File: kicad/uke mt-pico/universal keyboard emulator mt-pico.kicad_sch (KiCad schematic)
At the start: 0 parts

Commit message: first pcb floorplan
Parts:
- added C1, C2, C3, C6, C8: 10u, Capacitor_SMD:C_0805_2012Metric, symbol My Library:C_0805
- added C5: 100u, Capacitor_THT:CP_Radial_D5.0mm_P2.50mm, symbol Device:C_Polarized_Small
- added C7: 100n, Capacitor_SMD:C_0805_2012Metric, symbol My Library:C_0805
- added D1: L, LED_SMD:LED_1206_3216Metric, symbol My Library:D_1206
- added D2: +3V3, LED_SMD:LED_1206_3216Metric, symbol My Library:D_1206
- added D3: +5V, LED_SMD:LED_1206_3216Metric, symbol My Library:D_1206
- added D4: SM4001, Diode_SMD:D_SMA_Handsoldering, symbol Diode:SM4001
- added D5, D6, D7: NSVR0320MW2T1G, Diode_SMD:D_SOD-323_HandSoldering, symbol Diode:SM4001
- added H1, H2, H3, H4: MountingHole, MountingHole:MountingHole_2.2mm_M2, symbol Mechanical:MountingHole
- added J1: Mode Select, Connector_PinHeader_2.54mm:PinHeader_1x03_P2.54mm_Vertical, symbol Connector_Generic:Conn_01x03
- added J2: OLED Adapter, Connector_PinSocket_2.54mm:PinSocket_1x04_P2.54mm_Vertical, symbol Connector_Generic:Conn_01x04
- added J3: Serial, Connector_PinHeader_2.54mm:PinHeader_1x05_P2.54mm_Vertical, symbol Connector_Generic:Conn_01x05
- added J4: Conn_02x20_Odd_Even, Connector_PinHeader_2.54mm:PinHeader_2x20_P2.54mm_Vertical, symbol Connector_Generic:Conn_02x20_Odd_Even
- added J5: SWD, SAMTEC_FTSH-105-XX-X-DV, symbol FTSH-105-XX-X-DV:FTSH-105-XX-X-DV
- added J6: Pico VBUS, Connector_PinHeader_2.54mm:PinHeader_1x02_P2.54mm_Vertical, symbol Connector_Generic:Conn_01x02
- added R1, R9: 1M, Resistor_SMD:R_0805_2012Metric, symbol My Library:R_0805
- added R2, R3, R4: 1k, Resistor_SMD:R_0805_2012Metric, symbol My Library:R_0805
- added R5, R6, R7, R8: 10k, Resistor_SMD:R_0805_2012Metric, symbol My Library:R_0805
- added SW1: Reset Pico, Button_Switch_SMD:SW_SPST_PTS810, symbol Switch:SW_SPST
- added TP1, TP2, TP3: TestPoint_Harwin, My Libraries:Harwin-S1751-46-Test-Point, symbol My Library:TestPoint_Harwin
- added U1: MT8816, Package_DIP:DIP-40_W15.24mm_Socket_LongPads, symbol My Library:MT8816_40-Pin_DIP
- added U2, U3: 74HCT245, Package_SO:SOIC-20W_7.5x12.8mm_P1.27mm, symbol 74xx:74HC245
- added U4: Pico, My Libraries:RPi_Pico_W_Combined_SMD_TH, symbol RPi_Pico:Pico
- added U5: 74HCT595-VERIFY-FOOTPRINT, Package_SO:SO-16_3.9x9.9mm_P1.27mm, symbol 74xx:74HC595
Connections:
- new net: D3.1 (K), R4.1
- new net: R6.2, U3.1 (A->B)
- new net: D7.1 (K), U3.20 (VCC)
- new net: D2.1 (K), R3.1
- new net: D1.1 (K), R2.1
- new net: D6.1 (K), U2.20 (VCC)
- new net: D5.1 (K), U5.10 (~{SRCLR}), U5.16 (VCC)
- new net: R5.2, U2.1 (A->B)
- new net +3V3: C7.1, D2.2 (A), J4.38 (Pin_38), J5.01, U4.36 (3V3)
- new net +5V: C1.1, C2.1, C3.1, C5.1, C6.1, C8.1, D3.2 (A), D4.2 (A), D5.2 (A), D6.2 (A), D7.2 (A), J4.1 (Pin_1), J4.2 (Pin_2), R1.1, R7.1, R8.1, U1.40 (VDD)
- new net +5VA: D4.1 (K), J2.2 (Pin_2), J6.1 (Pin_1), U4.40 (VBUS)
- new net 245s_CE: R7.2, R8.2, U2.19 (CE), U3.19 (CE), U4.11 (GPIO8)
- new net 595_CLK: U4.5 (GPIO3), U5.11 (SRCLK)
- new net 595_DATA: U4.4 (GPIO2), U5.14 (SER)
- new net 595_Latch: U4.10 (GPIO7), U5.12 (RCLK)
- new net ADID: J4.37 (Pin_37), U4.32 (GPIO27_ADC1)
- new net AX0: U1.5 (AX0), U2.6 (A4)
- new net AX1: U1.22 (AX1), U2.3 (A1)
- new net AX2: U1.23 (AX2), U2.2 (A0)
- new net AX3: U1.4 (AX3), U2.7 (A5)
- new net AY0: U1.24 (AY0), U2.4 (A2)
- new net AY1: U1.25 (AY1), U2.5 (A3)
- new net AY2: U1.2 (AY2), U2.9 (A7)
- new net COL0: J4.3 (Pin_3), U1.33 (X0)
- new net COL1: J4.5 (Pin_5), U1.32 (X1)
- new net COL10: J4.25 (Pin_25), U1.12 (X10)
- new net COL11: J4.27 (Pin_27), U1.13 (X11)
- new net COL12: J4.29 (Pin_29), U1.27 (X12)
- new net COL13: J4.31 (Pin_31), U1.26 (X13)
- new net COL14: J4.33 (Pin_33), U1.6 (X14)
- new net COL15: J4.35 (Pin_35), U1.7 (X15)
- new net COL2: J4.7 (Pin_7), U1.31 (X2)
- new net COL3: J4.9 (Pin_9), U1.30 (X3)
- new net COL4: J4.11 (Pin_11), U1.29 (X4)
- new net COL5: J4.13 (Pin_13), U1.28 (X5)
- new net COL6: J4.15 (Pin_15), U1.8 (X6)
- new net COL7: J4.17 (Pin_17), U1.9 (X7)
- new net COL8: J4.21 (Pin_21), U1.10 (X8)
- new net COL9: J4.23 (Pin_23), U1.11 (X9)
- new net CS: U1.36 (CS), U3.9 (A7)
- new net DATA: U1.38 (DATA), U3.8 (A6)
- new net GND: C1.2, C2.2, C3.2, C5.2, C6.2, C7.2, C8.2, J1.2 (Pin_2), J2.1 (Pin_1), J3.1 (Pin_1), J4.39 (Pin_39), J4.40 (Pin_40), J5.03, J5.05, J5.09, J6.2 (Pin_2), R2.2, R3.2, R4.2, R5.1, R6.1, R9.2, SW1.2 (B), TP1.1, TP2.1, TP3.1, U1.16 (VSS), U1.20 (VEE), U2.10 (GND), U3.10 (GND), U4.13 (GND), U4.18 (GND), U4.23 (GND), U4.28 (GND), U4.3 (GND), U4.33 (AGND), U4.38 (GND), U4.8 (GND), U5.8 (GND)
- new net HID: J1.1 (Pin_1), U4.34 (GPIO28_ADC2)
- new net LED: D1.2 (A), U4.26 (GPIO20)
- new net OLED_SCL: J2.3 (Pin_3), U4.22 (GPIO17)
- new net OLED_SDA: J2.4 (Pin_4), U4.21 (GPIO16)
- new net RESET: U1.3 (RESET), U2.8 (A6)
- new net ROW0: J4.4 (Pin_4), U1.35 (Y0)
- new net ROW1: J4.6 (Pin_6), U1.37 (Y1)
- new net ROW2: J4.8 (Pin_8), U1.39 (Y2)
- new net ROW3: J4.10 (Pin_10), U1.1 (Y3)
- new net ROW4: J4.12 (Pin_12), U1.21 (Y4)
- new net ROW5: J4.14 (Pin_14), U1.19 (Y5)
- new net ROW6: J4.16 (Pin_16), U1.17 (Y6)
- new net ROW7: J4.18 (Pin_18), U1.15 (Y7)
- new net RUN: J5.10, SW1.1 (A), U4.30 (RUN)
- new net RX_2040: J3.4 (Pin_4), U4.2 (GPIO1)
- new net SH0: J4.22 (Pin_22), U5.15 (QA)
- new net SH1: J4.24 (Pin_24), U5.1 (QB)
- new net SH2: J4.26 (Pin_26), U5.2 (QC)
- new net SH3: J4.28 (Pin_28), U5.3 (QD)
- new net SH4: J4.30 (Pin_30), U5.4 (QE)
- new net SH5: J4.32 (Pin_32), U5.5 (QF)
- new net SH6: J4.34 (Pin_34), U5.6 (QG)
- new net SH7: J4.36 (Pin_36), U5.7 (QH)
- new net STROBE: U1.18 (STROBE), U3.3 (A1)
- new net SWCLK: J5.04, U4.41 (SWCLK)
- new net SWDIO: J5.02, U4.43 (SWDIO)
- new net Serial: J1.3 (Pin_3), U4.29 (GPIO22)
- new net TMEAS: R1.2, R9.1, U4.31 (GPIO26_ADC0)
- new net TX_2040: J3.5 (Pin_5), U4.1 (GPIO0)
- new net rpAX0: U2.14 (B4), U4.17 (GPIO13)
- new net rpAX1: U2.17 (B1), U4.14 (GPIO10)
- new net rpAX2: U2.18 (B0), U4.12 (GPIO9)
- new net rpAX3: U2.13 (B5), U4.19 (GPIO14)
- new net rpAY0: U2.16 (B2), U4.15 (GPIO11)
- new net rpAY1: U2.15 (B3), U4.16 (GPIO12)
- new net rpAY2: U2.11 (B7), U4.25 (GPIO19)
- new net rpCS: U3.11 (B7), U4.6 (GPIO4)
- new net rpDATA: U3.12 (B6), U4.7 (GPIO5)
- new net rpRESET: U2.12 (B6), U4.20 (GPIO15)
- new net rpSTROBE: U3.17 (B1), U4.9 (GPIO6)
- new net ~{595_OE}: U4.24 (GPIO18), U5.13 (~{OE})
- no-connect marks 0 -> 17
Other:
- note added: "* MT8816 selectable power between target and Pico * Buffers selectable power"
- note added: "16 x 8 (24 pins) Ground 5V 6 generic IO (pull-down/pull-up/driven)"

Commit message: Pre-route #1
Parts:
- added TP4, TP5, TP6: TestPoint, TestPoint:TestPoint_Pad_1.0x1.0mm, symbol Connector:TestPoint
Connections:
- net at U4.27 (GPIO21): now also TP5.1
- net at U4.37 (3V3_EN): now also TP4.1
- net at U4.39 (VSYS): now also TP6.1
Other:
- moved on the sheet: C1, C2, C3, C5, C6, C7, C8, D1, D2, D3, D5, D6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

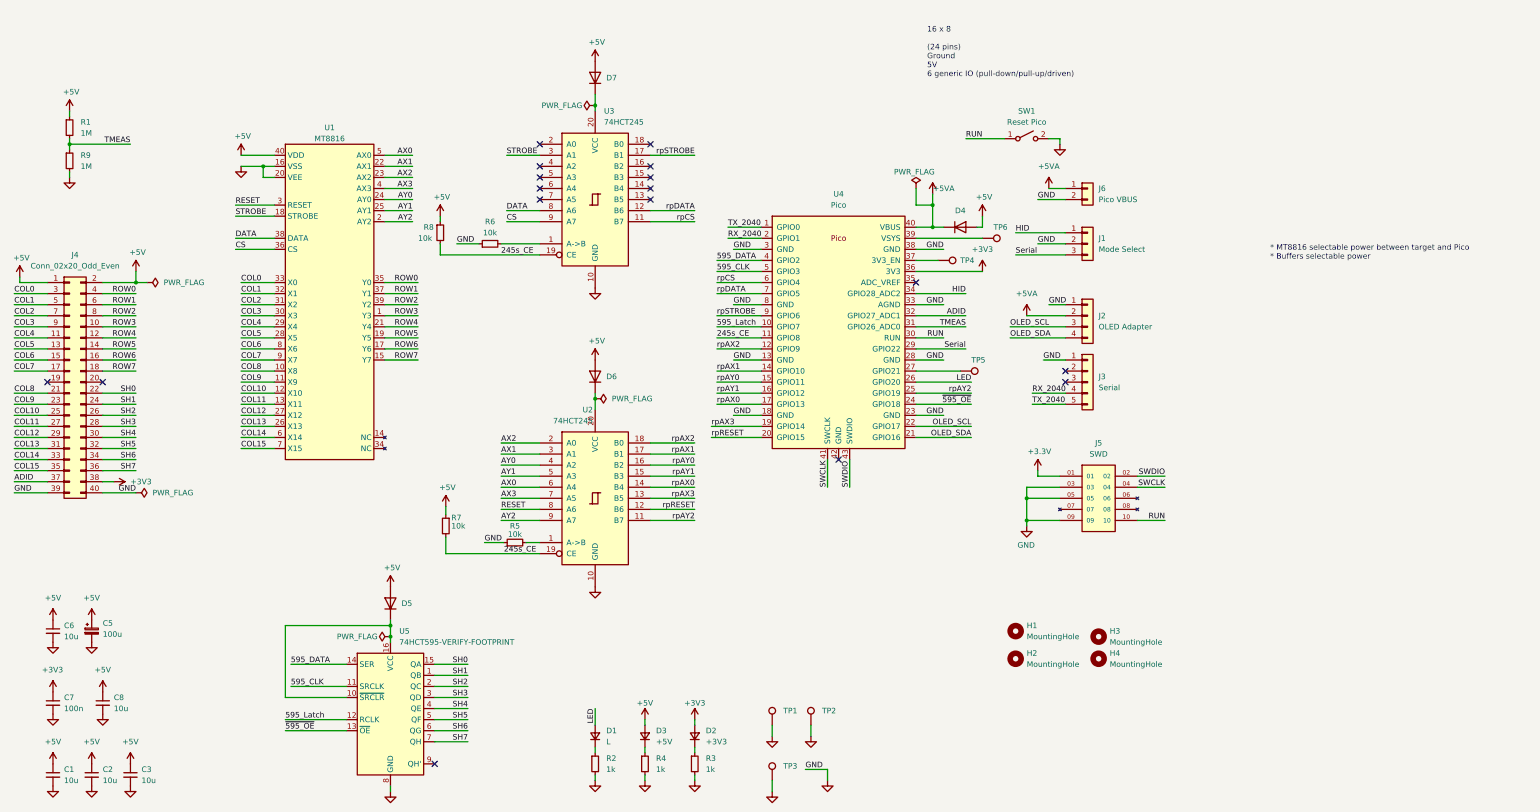
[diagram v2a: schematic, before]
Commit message: all but 5v routed
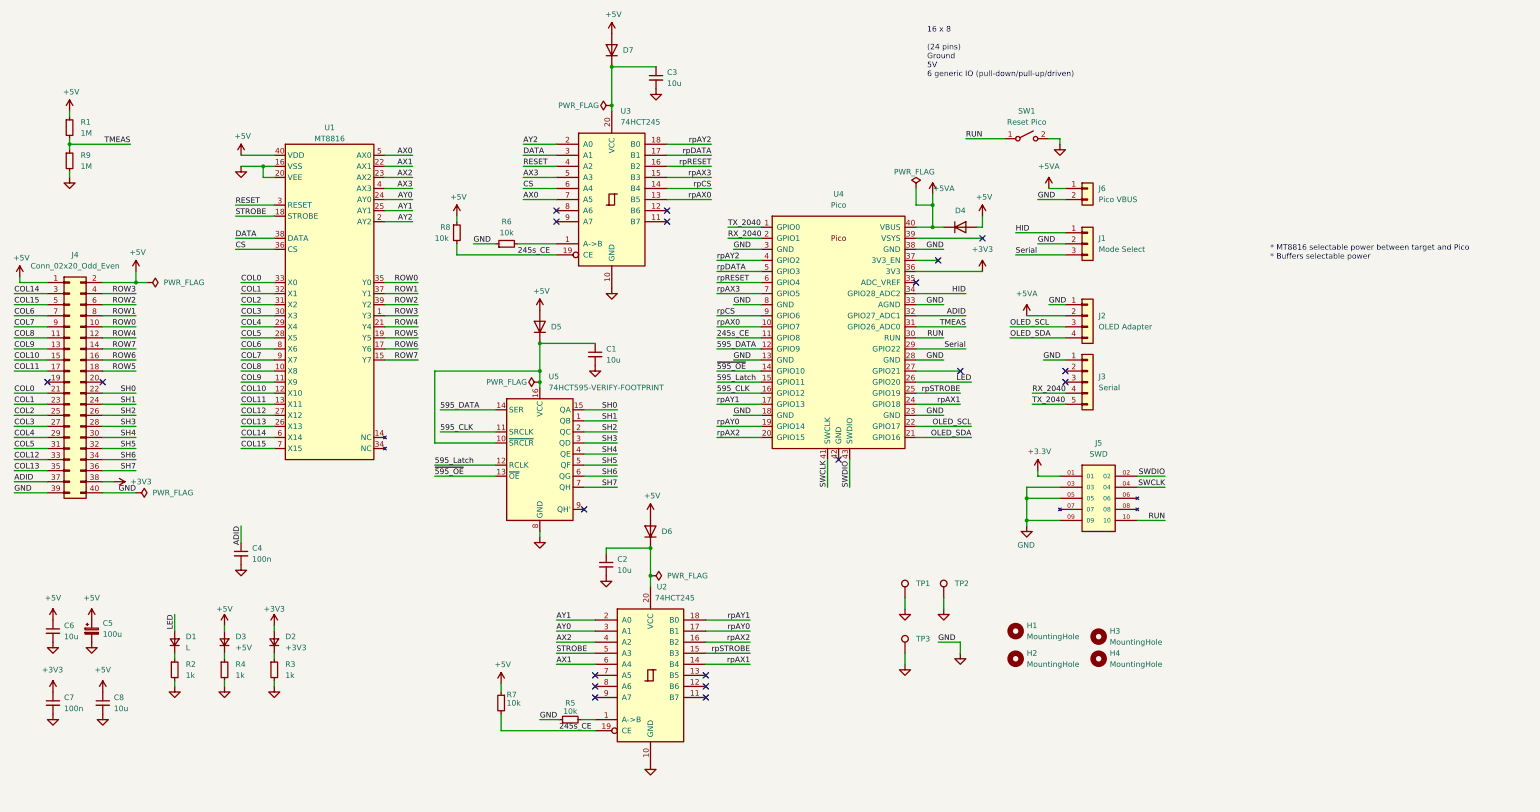
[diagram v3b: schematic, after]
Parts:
- removed TP4, TP5, TP6: TestPoint, TestPoint:TestPoint_Pad_1.0x1.0mm, symbol Connector:TestPoint
- added C4: 100n, Capacitor_SMD:C_0805_2012Metric, symbol My Library:C_0805
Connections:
- net +5V: no longer C1.1, C2.1, C3.1
- net 595_CLK: now also U4.16 (GPIO12); no longer U4.5 (GPIO3)
- net 595_DATA: now also U4.12 (GPIO9); no longer U4.4 (GPIO2)
- net 595_Latch: now also U4.15 (GPIO11); no longer U4.10 (GPIO7)
- net ADID: now also C4.1
- net AX0: now also U3.7 (A5); no longer U2.6 (A4)
- net AX1: now also U2.6 (A4); no longer U2.3 (A1)
- net AX2: now also U2.4 (A2); no longer U2.2 (A0)
- net AX3: now also U3.5 (A3); no longer U2.7 (A5)
- net AY0: now also U2.3 (A1); no longer U2.4 (A2)
- net AY1: now also U2.2 (A0); no longer U2.5 (A3)
- net AY2: now also U3.2 (A0); no longer U2.9 (A7)
- net COL0: now also J4.21 (Pin_21); no longer J4.3 (Pin_3)
- net COL1: now also J4.23 (Pin_23); no longer J4.5 (Pin_5)
- net COL10: now also J4.15 (Pin_15); no longer J4.25 (Pin_25)
- net COL11: now also J4.17 (Pin_17); no longer J4.27 (Pin_27)
- net COL12: now also J4.33 (Pin_33); no longer J4.29 (Pin_29)
- net COL13: now also J4.35 (Pin_35); no longer J4.31 (Pin_31)
- net COL14: now also J4.3 (Pin_3); no longer J4.33 (Pin_33)
- net COL15: now also J4.5 (Pin_5); no longer J4.35 (Pin_35)
- net COL2: now also J4.25 (Pin_25); no longer J4.7 (Pin_7)
- net COL3: now also J4.27 (Pin_27); no longer J4.9 (Pin_9)
- net COL4: now also J4.29 (Pin_29); no longer J4.11 (Pin_11)
- net COL5: now also J4.31 (Pin_31); no longer J4.13 (Pin_13)
- net COL6: now also J4.7 (Pin_7); no longer J4.15 (Pin_15)
- net COL7: now also J4.9 (Pin_9); no longer J4.17 (Pin_17)
- net COL8: now also J4.11 (Pin_11); no longer J4.21 (Pin_21)
- net COL9: now also J4.13 (Pin_13); no longer J4.23 (Pin_23)
- net CS: now also U3.6 (A4); no longer U3.9 (A7)
- net DATA: now also U3.3 (A1); no longer U3.8 (A6)
- net GND: now also C4.2
- net RESET: now also U3.4 (A2); no longer U2.8 (A6)
- net ROW0: now also J4.10 (Pin_10); no longer J4.4 (Pin_4)
- net ROW1: now also J4.8 (Pin_8); no longer J4.6 (Pin_6)
- net ROW2: now also J4.6 (Pin_6); no longer J4.8 (Pin_8)
- net ROW3: now also J4.4 (Pin_4); no longer J4.10 (Pin_10)
- net ROW5: now also J4.18 (Pin_18); no longer J4.14 (Pin_14)
- net ROW7: now also J4.14 (Pin_14); no longer J4.18 (Pin_18)
- net STROBE: now also U2.5 (A3); no longer U3.3 (A1)
- net rpAX0: now also U3.13 (B5), U4.10 (GPIO7); no longer U2.14 (B4), U4.17 (GPIO13)
- net rpAX1: now also U2.14 (B4), U4.24 (GPIO18); no longer U2.17 (B1), U4.14 (GPIO10)
- net rpAX2: now also U2.16 (B2), U4.20 (GPIO15); no longer U2.18 (B0), U4.12 (GPIO9)
- net rpAX3: now also U3.15 (B3), U4.7 (GPIO5); no longer U2.13 (B5), U4.19 (GPIO14)
- net rpAY0: now also U2.17 (B1), U4.19 (GPIO14); no longer U2.16 (B2), U4.15 (GPIO11)
- net rpAY1: now also U2.18 (B0), U4.17 (GPIO13); no longer U2.15 (B3), U4.16 (GPIO12)
- net rpAY2: now also U3.18 (B0), U4.4 (GPIO2); no longer U2.11 (B7), U4.25 (GPIO19)
- net rpCS: now also U3.14 (B4), U4.9 (GPIO6); no longer U3.11 (B7), U4.6 (GPIO4)
- net rpDATA: now also U3.17 (B1), U4.5 (GPIO3); no longer U3.12 (B6), U4.7 (GPIO5)
- net rpRESET: now also U3.16 (B2), U4.6 (GPIO4); no longer U2.12 (B6), U4.20 (GPIO15)
- net rpSTROBE: now also U2.15 (B3), U4.25 (GPIO19); no longer U3.17 (B1), U4.9 (GPIO6)
- net ~{595_OE}: now also U4.14 (GPIO10); no longer U4.24 (GPIO18)
- net at D7.1 (K), U3.20 (VCC): now also C3.1
- net at D6.1 (K), U2.20 (VCC): now also C2.1
- net at D5.1 (K), U5.10 (~{SRCLR}), U5.16 (VCC): now also C1.1
- no-connect marks 17 -> 20
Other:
- moved on the sheet: C1, C2, C3, D1, D2, D3, D5, D6, D7, R2, R3, R4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

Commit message: final pcb - not yet submitted to fab though
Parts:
- removed H1, H2, H3: MountingHole, MountingHole:MountingHole_2.2mm_M2, symbol Mechanical:MountingHole
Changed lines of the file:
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@@
     (pin "2")
-  )
-  (symbol (lib_id "Mechanical:MountingHole") (at 247.65 161.29 0) (unit 1)
-    (in_bom yes) (on_board yes)
-    (property "Reference" "H2" (id 0) (at 250.19 160.0199 0)
-      (effects (font (size 1.27 1.27)) (justify left))
-    )
-    (property "Value" "MountingHole" (id 1) (at 250.19 162.5599 0)
-      (effects (font (size 1.27 1.27)) (justify left))
-    )
-    (property "Footprint" "MountingHole:MountingHole_2.2mm_M2" (id 2) (at 241.3 156.21 0)
-      (effects (font (size 1.27 1.27)) hide)
-    )
-    (property "Datasheet" "~" (id 3) (at 247.65 161.29 0)
-      (effects (font (size 1.27 1.27)) hide)
-    )
   )
   (symbol (lib_id "My Library:C_0805") (at 26.67 171.45 0) (unit 1)
@@
     )
     (pin "1")
-  )
-  (symbol (lib_id "Mechanical:MountingHole") (at 266.7 156.21 0) (unit 1)
-    (in_bom yes) (on_board yes)
-    (property "Reference" "H3" (id 0) (at 269.24 154.9399 0)
-      (effects (font (size 1.27 1.27)) (justify left))
-    )
-    (property "Value" "MountingHole" (id 1) (at 269.24 157.4799 0)
-      (effects (font (size 1.27 1.27)) (justify left))
-    )
-    (property "Footprint" "MountingHole:MountingHole_2.2mm_M2" (id 2) (at 260.35 151.13 0)
-      (effects (font (size 1.27 1.27)) hide)
-    )
-    (property "Datasheet" "~" (id 3) (at 266.7 156.21 0)
-      (effects (font (size 1.27 1.27)) hide)
-    )
   )
   (symbol (lib_id "Mechanical:MountingHole") (at 266.7 161.29 0) (unit 1)
@@
     (pin "1")
   )
-  (symbol (lib_id "Mechanical:MountingHole") (at 247.65 154.94 0) (unit 1)
-    (in_bom yes) (on_board yes)
-    (property "Reference" "H1" (id 0) (at 250.19 153.6699 0)
-      (effects (font (size 1.27 1.27)) (justify left))
-    )
-    (property "Value" "MountingHole" (id 1) (at 250.19 156.2099 0)
-      (effects (font (size 1.27 1.27)) (justify left))
-    )
-    (property "Footprint" "MountingHole:MountingHole_2.2mm_M2" (id 2) (at 241.3 149.86 0)
-      (effects (font (size 1.27 1.27)) hide)
-    )
-    (property "Datasheet" "~" (id 3) (at 247.65 154.94 0)
-      (effects (font (size 1.27 1.27)) hide)
-    )
-  )
   (symbol (lib_id "power:+5VA") (at 255.27 53.34 0) (unit 1)
     (in_bom yes) (on_board yes) (fields_autoplaced)
@@
       (reference "D7") (unit 1) (value "NSVR0320MW2T1G") (footprint "Diode_SMD:D_SOD-323_HandSoldering")
     )
-    (path "/f76c58c0-c659-4270-9cda-a6838a4fc4e5"
-      (reference "H1") (unit 1) (value "MountingHole") (footprint "MountingHole:MountingHole_2.2mm_M2")
-    )
-    (path "/2ae752e6-9aaf-4d2b-9686-04bccb313236"
-      (reference "H2") (unit 1) (value "MountingHole") (footprint "MountingHole:MountingHole_2.2mm_M2")
-    )
-    (path "/5c8c765f-7979-4bbd-9187-9c59bb5e1f4a"
-      (reference "H3") (unit 1) (value "MountingHole") (footprint "MountingHole:MountingHole_2.2mm_M2")
-    )
     (path "/5f6e96f6-eaa3-4caa-9a3d-41990b868870"
